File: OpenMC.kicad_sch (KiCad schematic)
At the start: 14 parts, among them J1 Motor Digital, J2 USB-C, J3 CAN, J4 Controller, J5 Motor Analog

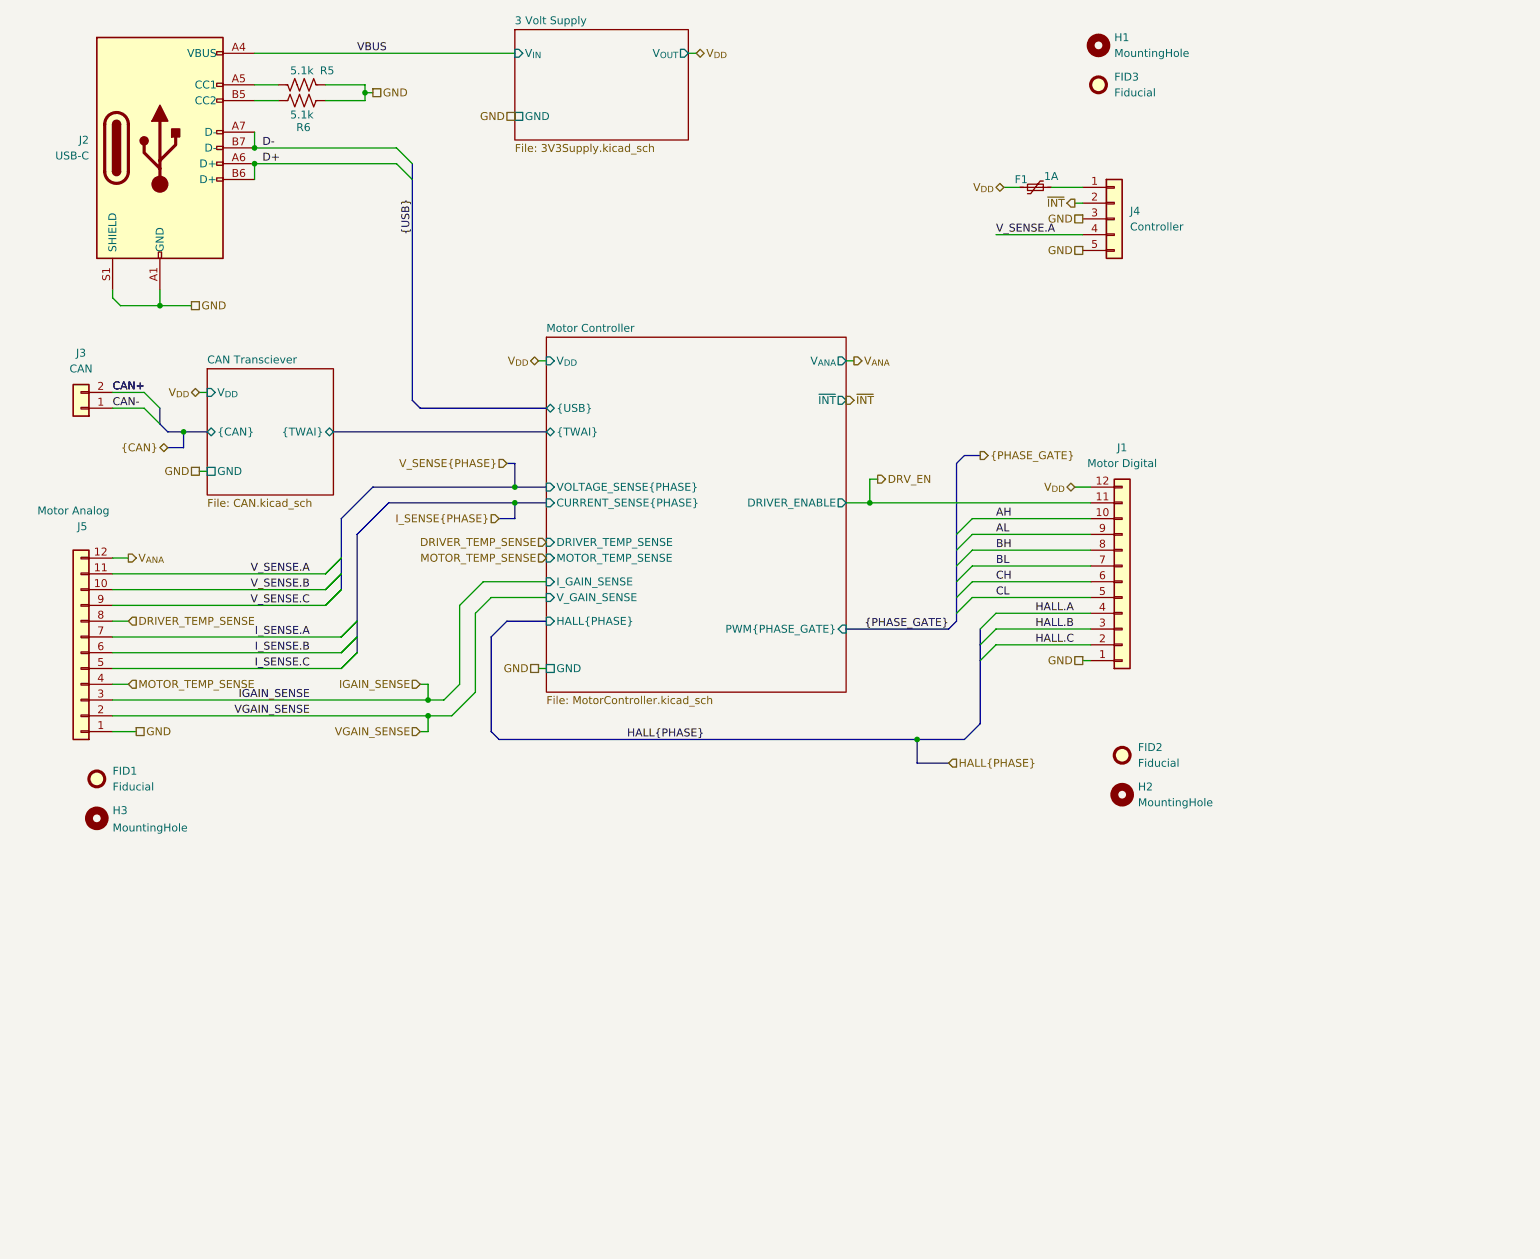
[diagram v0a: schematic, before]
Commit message: updated to external adc
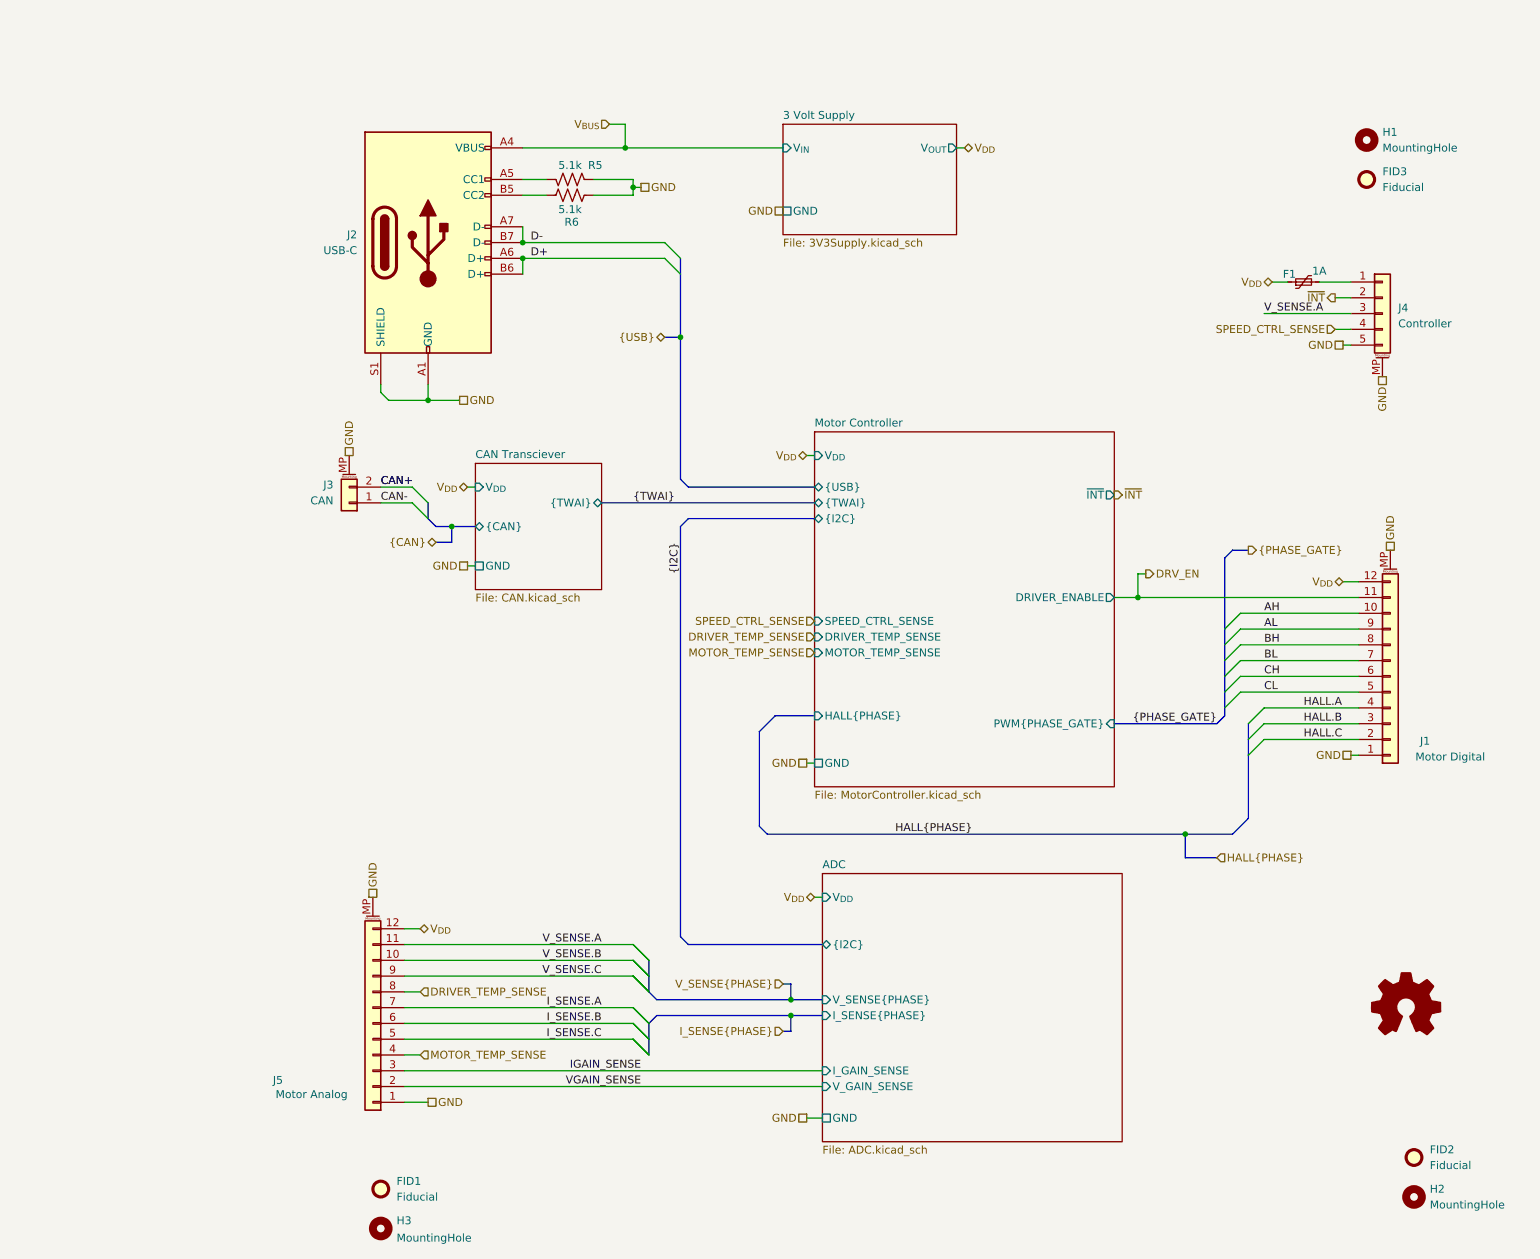
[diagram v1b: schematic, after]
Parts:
- added SYM1: Logo_Open_Hardware_Small, Symbol:OSHW-Symbol_6.7x6mm_SilkScreen, symbol Graphic:Logo_Open_Hardware_Small
- F1: symbol Device:Polyfuse_Small -> OpenMC:Polyfuse_Small; MPN (none) -> 3412.0115.11
- FID1, FID2, FID3: symbol Mechanical:Fiducial -> OpenMC:Fiducial
- H1, H2, H3: symbol Mechanical:MountingHole -> OpenMC:MountingHole
- J1, J5: symbol Connector_Generic:Conn_01x12 -> Connector_Generic_MountingPin:Conn_01x12_MountingPin; MPN (none) -> SM12B-SRSS-TB(LF)(SN)
- J2: symbol Connector:USB_C_Receptacle_USB2.0_14P -> OpenMC:USB_C_Receptacle_USB2.0_14P; MPN (none) -> USB4105-GF-A-120.
- J3: symbol Connector_Generic:Conn_01x02 -> Connector_Generic_MountingPin:Conn_01x02_MountingPin; MPN (none) -> SM02B-SRSS-TB(LF)(SN)
- J4: symbol Connector_Generic:Conn_01x05 -> Connector_Generic_MountingPin:Conn_01x05_MountingPin; MPN (none) -> SM05B-SRSS-TB(LF)(SN)
- R5, R6: symbol Device:R_US -> OpenMC:R_US; MPN (none) -> ERJ3RBD5101V
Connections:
- net V_{ANA} is gone; now on net V_{DD}: J5.12 (Pin_12)
- net GND: now also J1.MP (MountPin), J3.MP (MountPin), J4.MP (MountPin), J5.MP (MountPin); no longer J4.3 (Pin_3)
- net V_SENSE.A: now also J4.3 (Pin_3); no longer J4.4 (Pin_4)
- net VBUS renamed V_{BUS}
- new net SPEED_CTRL_SENSE: J4.4 (Pin_4)
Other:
- added sheet ADC (ADC.kicad_sch)
- sheet Motor Controller  ports: added SPEED_CTRL_SENSE, {I2C}; removed CURRENT_SENSE{PHASE}, I_GAIN_SENSE, VOLTAGE_SENSE{PHASE}, V_GAIN_SENSE, V_{ANA}
- company: Nebula Labs -> (none)
- moved on the sheet: F1, FID1, FID2, FID3, H1, H2, H3, J2, R5, R6
